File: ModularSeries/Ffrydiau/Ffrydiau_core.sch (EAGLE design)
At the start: 90 parts, among them IC3 556_DUALTIMERDIL14, Q1 2N3906, Q2 2N3904, Q3 2N3904, Q4 2N7000, Q5 2N7000, Q6 2N3904, Q7 2N3904, SW1 3XWIREPAD

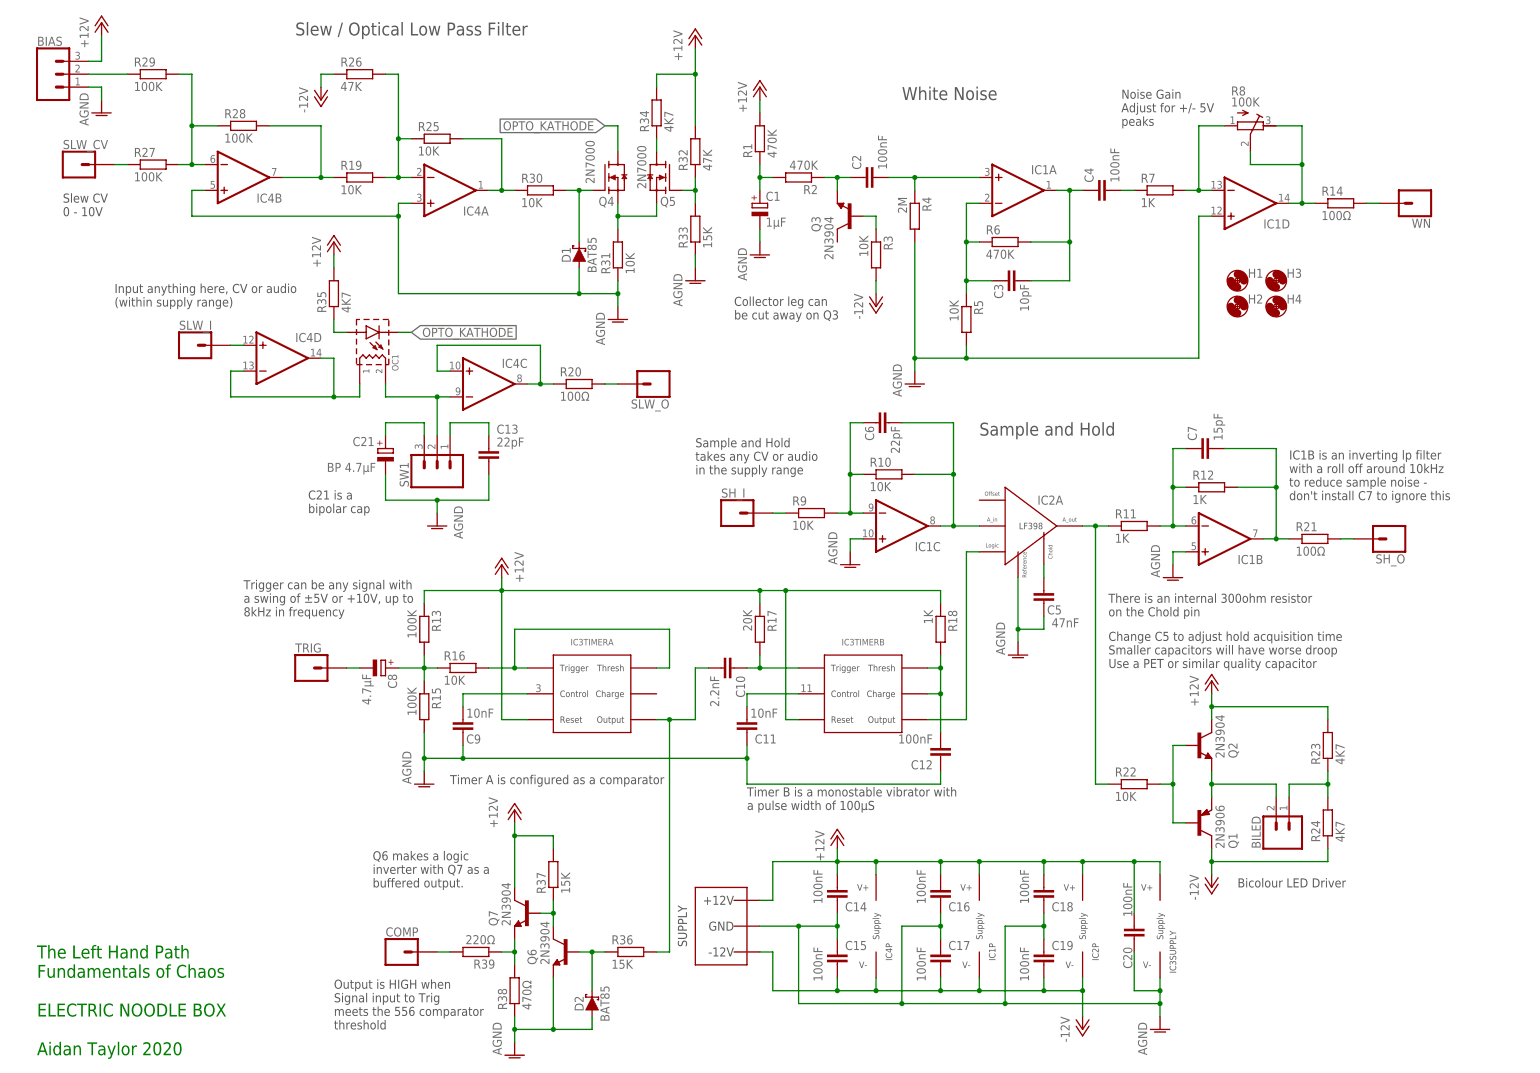
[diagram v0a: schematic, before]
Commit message: Portals BOM update, Ffrydiau project added
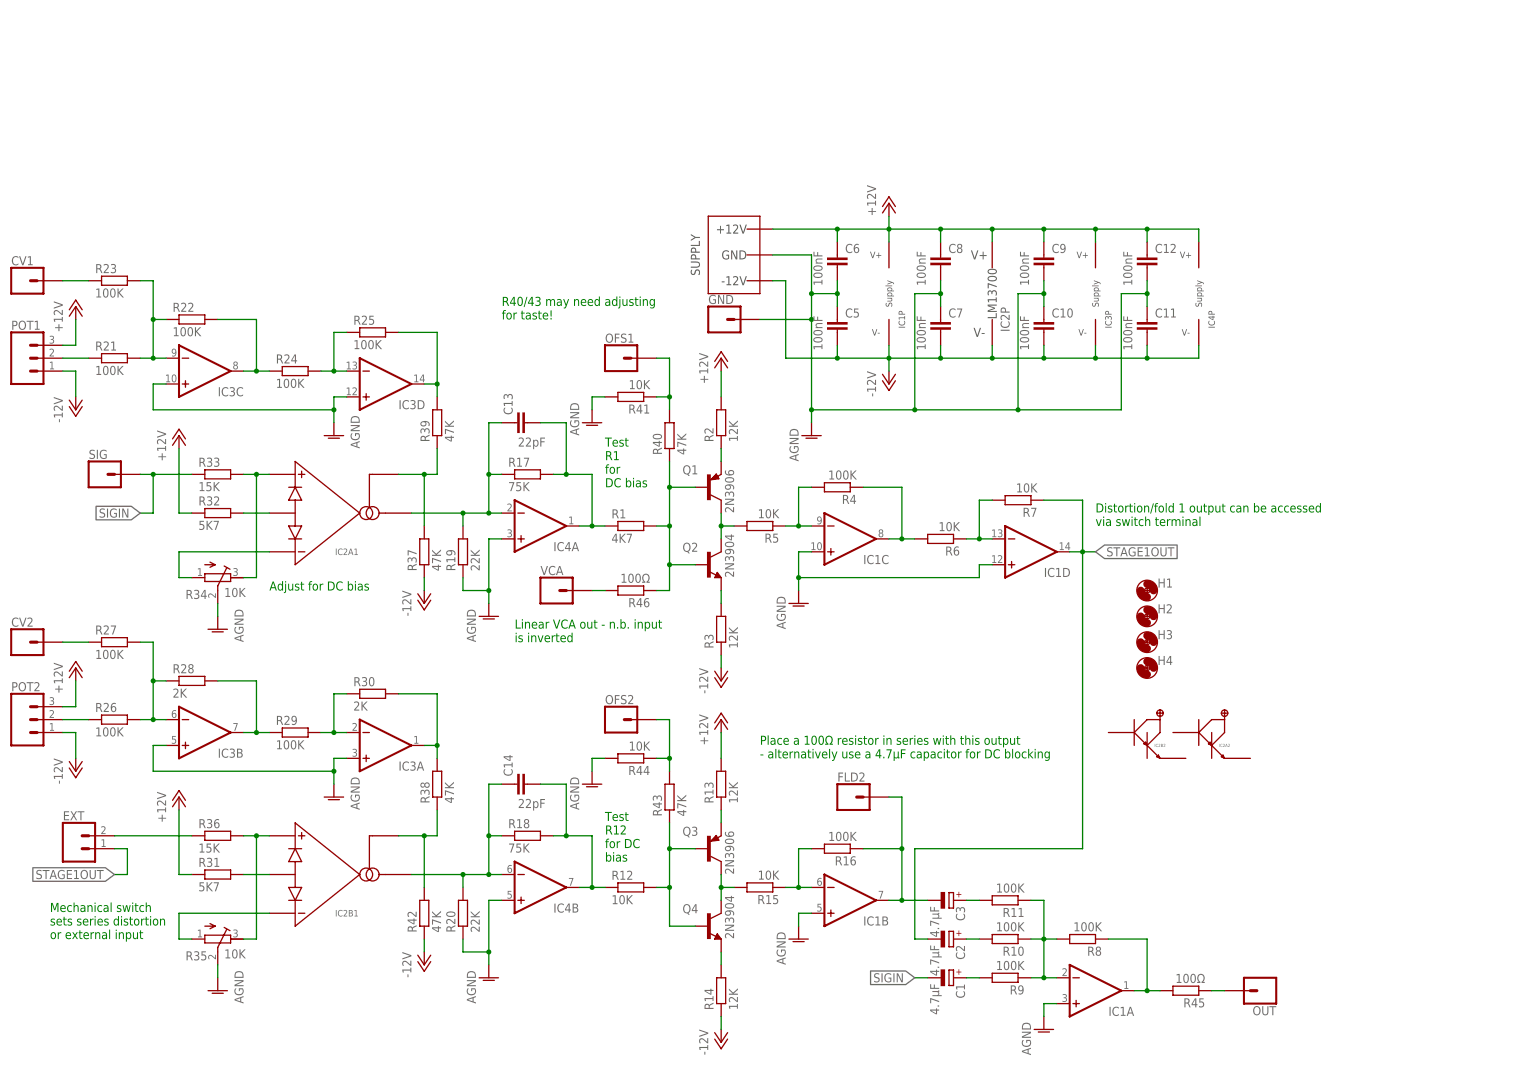
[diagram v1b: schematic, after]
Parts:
- removed BIAS, SW1: 3XWIREPAD, ElectricNoodleBox:3XWIREPAD
- removed BILED: 2XWIREPAD, ElectricNoodleBox:2XWIREPAD
- removed C15, C16, C17, C18, C19, C20, C4: 100nF, rcl:C-EU050-025X075
- removed C21: BP 4.7µF, rcl:CPOL-EUE2-5
- removed COMP, SH_I, SH_O, SLW_CV, SLW_I, SLW_O, TRIG, WN: 1XWIREPAD, ElectricNoodleBox:1XWIREPAD
- removed D1, D2: BAT85, ElectricNoodleBox:SCHOTTKY_DO35
- removed OC1: OPTOCOUPLERSILONEX, ElectricNoodleBox:OPTOCOUPLERSILONEX
- removed Q5: 2N7000, ElectricNoodleBox:2N7000
- removed Q6, Q7: 2N3904, transistor:2N3904
- added CV1, CV2, FLD2, GND, OFS1, OFS2, OUT, SIG, VCA: 1XWIREPAD, ElectricNoodleBox:1XWIREPAD
- added EXT: 2XWIREPAD, ElectricNoodleBox:2XWIREPAD
- added POT1, POT2: 3XWIREPAD, ElectricNoodleBox:3XWIREPAD
- added R40, R42, R43: 47K, rcl:R-EU_0207/10
- added R41, R44: 10K, rcl:R-EU_0207/10
- added R45, R46: 100Ω, rcl:R-EU_0207/10
- C1: value 1µF -> 4.7µF; device rcl:CPOL-EUE2-5 -> rcl:CPOL-EUE2,5-6E
- C10: value 2.2nF -> 100nF
- C11, C9: value 10nF -> 100nF
- C14: value 100nF -> 22pF
- C2: value 100nF -> 4.7µF; device rcl:C-EU050-025X075 -> rcl:CPOL-EUE2,5-6E
- C3: value 10pF -> 4.7µF; device rcl:C-EU050-025X075 -> rcl:CPOL-EUE2,5-6E
- C5: value 47nF -> 100nF
- C6: value 22pF -> 100nF
- C7: value 15pF -> 100nF
- C8: value 4.7µF -> 100nF; device rcl:CPOL-EUE2-5 -> rcl:C-EU050-025X075
- IC2: device ElectricNoodleBox:LF398 -> ElectricNoodleBox:LM13700DIL
- IC3: value 556_DUALTIMERDIL14 -> (none); device ElectricNoodleBox:556_DUALTIMERDIL14 -> ElectricNoodleBox:TL0X4DIL
- IC4: device ElectricNoodleBox:TL0X4DIL -> ElectricNoodleBox:TL0X2DIL
- Q2: device transistor:2N3904 -> transistor-npn:2N3904
- Q3: value 2N3904 -> 2N3906; device transistor:2N3904 -> transistor-pnp:2N3906
- Q4: value 2N7000 -> 2N3904; device ElectricNoodleBox:2N7000 -> transistor-npn:2N3904
- R1: value 470K -> 4K7; device rcl:R-EU_0207/7 -> rcl:R-EU_0207/10
- R10, R16, R22, R25, R9: value 10K -> 100K; device rcl:R-EU_0207/7 -> rcl:R-EU_0207/10
- R11: value 1K -> 100K; device rcl:R-EU_0207/7 -> rcl:R-EU_0207/10
- R12, R7: value 1K -> 10K; device rcl:R-EU_0207/7 -> rcl:R-EU_0207/10
- R13: value 100K -> 12K; device rcl:R-EU_0207/7 -> rcl:R-EU_0207/10
- R14: value 100Ω -> 12K; device rcl:R-EU_0207/7 -> rcl:R-EU_0207/10
- R15: value 100K -> 10K; device rcl:R-EU_0207/7 -> rcl:R-EU_0207/10
- R17: value 20K -> 75K; device rcl:R-EU_0207/7 -> rcl:R-EU_0207/10
- R18: value 1K -> 75K; device rcl:R-EU_0207/7 -> rcl:R-EU_0207/10
- R19: value 10K -> 22K; device rcl:R-EU_0207/7 -> rcl:R-EU_0207/10
- R2: value 470K -> 12K; device rcl:R-EU_0207/7 -> rcl:R-EU_0207/10
- R20: value 100Ω -> 22K; device rcl:R-EU_0207/7 -> rcl:R-EU_0207/10
- R21: value 100Ω -> 100K; device rcl:R-EU_0207/7 -> rcl:R-EU_0207/10
- R23, R24: value 4K7 -> 100K; device rcl:R-EU_0207/7 -> rcl:R-EU_0207/10
- R26: value 47K -> 100K; device rcl:R-EU_0207/7 -> rcl:R-EU_0207/10
- R27, R29, R33, R36, R5: device rcl:R-EU_0207/7 -> rcl:R-EU_0207/10
- R28: value 100K -> 2K; device rcl:R-EU_0207/7 -> rcl:R-EU_0207/10
- R3: value 10K -> 12K; device rcl:R-EU_0207/7 -> rcl:R-EU_0207/10
- R30: value 10K -> 2K; device rcl:R-EU_0207/7 -> rcl:R-EU_0207/10
- R31: value 10K -> 5K7; device rcl:R-EU_0207/7 -> rcl:R-EU_0207/10
- R32: value 47K -> 5K7; device rcl:R-EU_0207/7 -> rcl:R-EU_0207/10
- R34, R35: value 4K7 -> 10K; device rcl:R-EU_0207/7 -> rcl:R-TRIMM3296W
- R37: value 15K -> 47K; device rcl:R-EU_0207/7 -> rcl:R-EU_0207/10
- R38: value 470Ω -> 47K; device rcl:R-EU_0207/7 -> rcl:R-EU_0207/10
- R39: value 220Ω -> 47K; device rcl:R-EU_0207/7 -> rcl:R-EU_0207/10
- R4: value 2M -> 100K; device rcl:R-EU_0207/7 -> rcl:R-EU_0207/10
- R6: value 470K -> 10K; device rcl:R-EU_0207/7 -> rcl:R-EU_0207/10
- R8: device rcl:R-TRIMM3296W -> rcl:R-EU_0207/10
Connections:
- removed net N$48: BIAS.2, R29.1
- removed net N$49: Q6.C, Q7.B, R37.1
- removed net N$50: Q7.E, R38.2, R39.1
- removed net N$51: COMP.1, R39.2
- removed net N$52: D2.C, Q6.B, R36.1
- removed net OPTO_KATHODE: OC1.K, Q4.D
- new net SIGIN: C1.-, R33.1, SIG.1
- new net STAGE1OUT: C2.-, EXT.1, IC1D.OUT, R7.1
- net +12V: now also C12.1, C6.1, C8.1, C9.1, IC3P.V+, POT1.3, POT2.3, R13.2, R2.2, R31.1, R32.1; no longer BIAS.3, C14.2, C16.2, C18.2, C20.2, IC3SUPPLY.V+, IC3TIMERA.RESET, IC3TIMERB.RESET, Q2.C, Q7.C, R1.2, R13.1, R17.1, R18.1, R23.2, R32.2, R34.2, R35.2, R37.2
- net -12V: now also C10.2, C11.2, C5.2, C7.2, IC3P.V-, POT1.1, POT2.1, R14.1, R3.1, R37.1, R42.1; no longer C15.1, C17.1, C19.1, Q1.C, R24.1, R26.1, R3.2
- net AGND: now also C10.1, C12.2, C6.2, C7.1, C8.2, C9.2, GND.1, IC1A.+IN, IC3A.+IN, IC3B.+IN, IC3C.+IN, IC3D.+IN, R19.1, R20.1, R34.S, R35.S, R41.2, R44.2; no longer BIAS.1, C1.-, C12.1, C13.1, C14.1, C15.2, C16.1, C17.2, C18.1, C19.2, C20.1, C21.-, C9.1, D1.A, D2.A, IC2A.REFERENCE, IC3SUPPLY.V-, Q6.E, R15.2, R31.1, R33.1, R38.1, R4.2, R5.2
- net N$1: now also Q1.B, Q2.B, R1.2, R40.1, R46.1; no longer C1.+, R1.1, R2.2
- net N$10: now also C3.+, R11.2; no longer C6.1, IC1C.-IN, R10.1, R9.2
- net N$11: now also C2.+; no longer C6.2, IC1C.OUT, IC2A.ANALOG_IN
- net N$12: now also C1.+, R9.2; no longer C5.2, IC2A.CH
- net N$13: now also IC1A.-IN, R10.1, R8.2, R9.1; no longer IC2A.ANALOG_OUT, R22.1
- net N$14: now also IC1A.OUT, R45.2, R8.1; no longer C7.1, IC1B.-IN, R11.2, R12.1
- net N$15: now also Q3.B, Q4.B, R43.1; no longer C7.2, IC1B.OUT, R21.1
- net N$16: now also Q3.E, R13.1; no longer R9.1, SH_I.1
- net N$17: now also Q4.E, R14.2; no longer C10.2, IC3TIMERA.OUTPUT, R36.2
- net N$18: now also Q3.C, Q4.C, R15.2; no longer C8.+, R13.2, R15.1, R16.1
- net N$19: now also IC1B.-IN, R15.1; no longer IC3TIMERA.THRESHOLD, IC3TIMERA.TRIGGER
- net N$2: now also Q1.E; no longer C2.1, Q3.E
- net N$20: now also C3.-, FLD2.1, IC1B.OUT, R16.1; no longer R14.2, WN.1
- net N$21: now also C14.1, IC2B1.AMPOUT, IC4B.-IN, R18.1, R20.2; no longer C9.2, IC3TIMERA.CONT
- net N$22: now also C13.1, IC2A1.AMPOUT, IC4A.-IN, R17.1, R19.2; no longer C10.1, IC3TIMERB.TRIGGER, R17.2
- net N$23: now also C14.2, IC4B.OUT, R12.1, R18.2; no longer C11.2, IC3TIMERB.CONT
- net N$24: now also IC3C.-IN, R21.2, R22.1, R23.2; no longer C12.2, IC3TIMERB.DISCHARGE, IC3TIMERB.THRESHOLD, R18.2
- net N$25: now also IC3C.OUT, R22.2, R24.1; no longer IC2A.LOGIC, IC3TIMERB.OUTPUT
- net N$26: now also IC3D.-IN, R24.2, R25.1; no longer C8.-, TRIG.1
- net N$27: now also IC3D.OUT, R25.2, R39.2; no longer IC4D.+IN, SLW_I.1
- net N$28: now also CV2.1, R27.1; no longer IC4D.-IN, IC4D.OUT, OC1.R1
- net N$29: now also IC3A.OUT, R30.2, R38.2; no longer IC4B.OUT, R19.1, R28.2
- net N$3: now also Q2.E, R3.2; no longer Q3.B, R3.1
- net N$30: now also POT1.2, R21.1; no longer IC4C.-IN, OC1.R2, SW1.2
- net N$31: now also IC3A.-IN, R29.2, R30.1; no longer IC4C.+IN, IC4C.OUT, R20.1
- net N$32: now also CV1.1, R23.1; no longer R20.2, SLW_O.1
- net N$33: now also IC3B.OUT, R28.2, R29.1; no longer R21.2, SH_O.1
- net N$34: now also IC3B.-IN, R26.2, R27.2, R28.1; no longer Q1.B, Q2.B, R22.2
- net N$35: now also IC2B1.AMP+, R35.E, R36.2; no longer BILED.2, Q1.E, Q2.E
- net N$36: now also IC2B1.AMP-, R35.A; no longer BILED.1, R23.1, R24.2
- net N$37: now also IC2B1.DIODES, R31.2; no longer IC4A.-IN, R19.2, R25.1, R26.2
- net N$38: now also IC2A1.DIODES, R32.2; no longer IC4B.-IN, R27.2, R28.1, R29.2
- net N$39: now also IC2A1.AMPBIAS, R37.2, R39.1; no longer IC4A.OUT, R25.2, R30.1
- net N$4: now also Q1.C, Q2.C, R5.2; no longer C2.2, IC1A.+IN, R4.1
- net N$40: now also POT2.2, R26.1; no longer D1.C, Q4.G, R30.2
- net N$41: now also IC2A1.AMP+, R33.2, R34.E; no longer Q4.S, Q5.S, R31.2
- net N$42: now also IC2A1.AMP-, R34.A; no longer C21.+, SW1.3
- net N$43: now also IC2B1.AMPBIAS, R38.1, R42.2; no longer Q5.G, R32.1, R33.2
- net N$44: now also OFS1.1, R40.2, R41.1; no longer Q5.D, R34.1
- net N$45: now also OFS2.1, R43.2, R44.1; no longer OC1.A, R35.1
- net N$46: now also R46.2, VCA.1; no longer C13.2, SW1.1
- net N$47: now also EXT.2, R36.1; no longer R27.1, SLW_CV.1
- net N$5: now also IC1C.-IN, R4.2; no longer C3.1, IC1A.-IN, R6.1
- net N$6: now also IC1C.OUT, R4.1; no longer C3.2, C4.1, IC1A.OUT
- net N$7: now also IC1D.-IN, R6.1, R7.2; no longer C4.2, R7.1
- net N$8: now also OUT.1, R45.1; no longer IC1D.-IN, R7.2, R8.A
- net N$9: now also C13.2, IC4A.OUT, R1.1, R17.2; no longer IC1D.OUT, R14.1, R8.E, R8.S
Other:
- note added: "Adjust for DC bias"
- note added: "Distortion/fold 1 output can be accessed via switch terminal"
- note added: "Linear VCA out - n.b. input is inverted"
- note added: "Mechanical switch sets series distortion or external input"
- note added: "Place a 100Ω resistor in series with this output - alternatively use a 4.7µF capacitor for DC blocking"
- note added: "R40/43 may need adjusting for taste!"
- note added: "Test R1 for DC bias"
- note added: "Test R12 for DC bias"
- note removed: "Bicolour LED Driver"
- note removed: "C21 is a bipolar cap"
- note removed: "Change C5 to adjust hold acquisition time Smaller capacitors will have worse droop Use a PET or similar quality capacitor"
- note removed: "Collector leg can be cut away on Q3"
- note removed: "IC1B is an inverting lp filter with a roll off around 10kHz to reduce sample noise - don't install C7 to ignore this"
- note removed: "Input anything here, CV or audio (within supply range)"
- note removed: "Noise Gain Adjust for +/- 5V peaks"
- note removed: "Output is HIGH when Signal input to Trig meets the 556 comparator threshold"
- note removed: "Q6 makes a logic inverter with Q7 as a buffered output."
- note removed: "Sample and Hold"
- note removed: "Sample and Hold takes any CV or audio in the supply range"
- note removed: "Slew / Optical Low Pass Filter"
- note removed: "Slew CV 0 - 10V"
- note removed: "The Left Hand Path Fundamentals of Chaos ELECTRIC NOODLE BOX Aidan Taylor 2020"
- note removed: "There is an internal 300ohm resistor on the Chold pin"
- note removed: "Timer A is configured as a comparator"
- note removed: "Timer B is a monostable vibrator with a pulse width of 100µS"
- note removed: "Trigger can be any signal with a swing of ±5V or +10V, up to 8kHz in frequency"
- note removed: "White Noise"
- moved on the sheet: C1, C10, C11, C12, C13, C14, C5, C6, C7, C9, H1, H2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

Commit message: Ffrydiau renders for core PCB added
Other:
- note added: "Ffrydiau v1.0 Complex Wave Distortion Module Aidan Taylor 2020 ELECTRIC NOODLE BOX"
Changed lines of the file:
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@@
 sets series distortion
 or external input</text>
+<text x="127" y="0" size="2.54" layer="91">Ffrydiau v1.0
+Complex Wave Distortion Module
+Aidan Taylor 2020
+ELECTRIC NOODLE BOX</text>
 </plain>
 <instances>

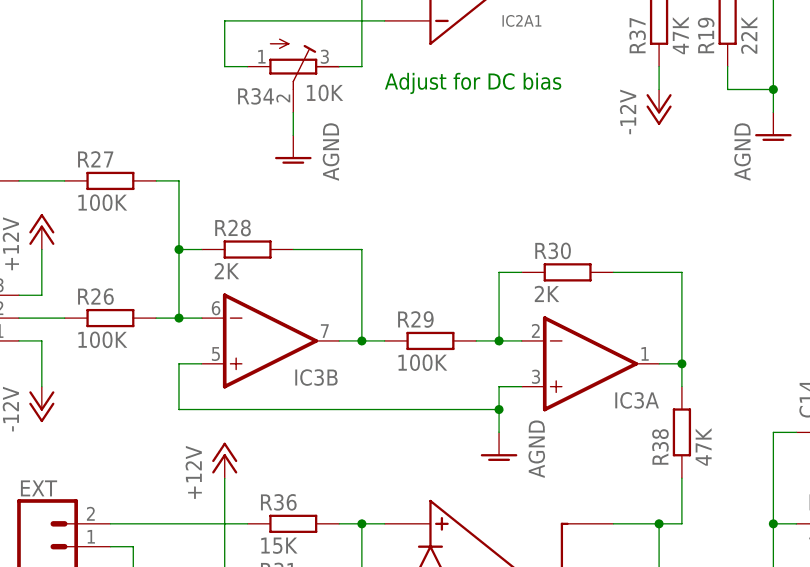
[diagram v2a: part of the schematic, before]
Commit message: Ffrydiau BOMs added
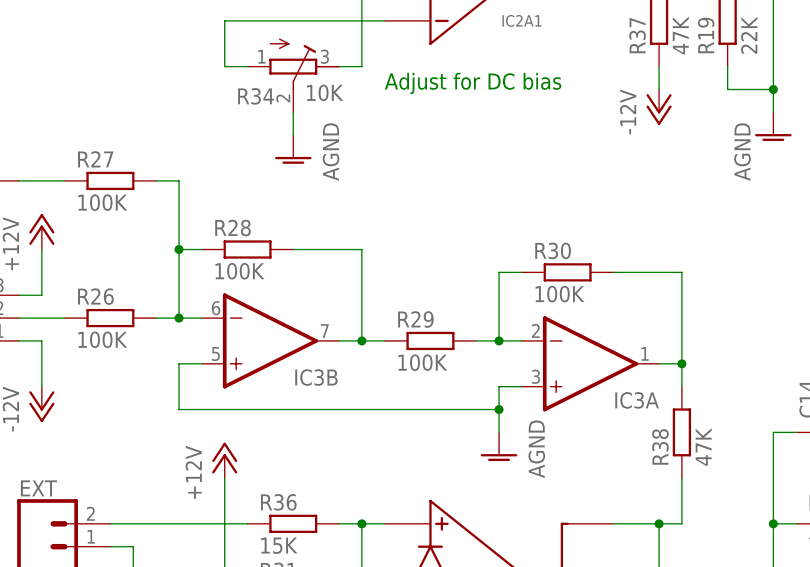
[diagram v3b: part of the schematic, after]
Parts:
- R28, R30: value 2K -> 100K
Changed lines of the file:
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@@
 <part name="R26" library="rcl" library_urn="urn:adsk.eagle:library:334" deviceset="R-EU_" device="0207/10" package3d_urn="urn:adsk.eagle:package:23491/2" value="100K"/>
 <part name="R27" library="rcl" library_urn="urn:adsk.eagle:library:334" deviceset="R-EU_" device="0207/10" package3d_urn="urn:adsk.eagle:package:23491/2" value="100K"/>
-<part name="R28" library="rcl" library_urn="urn:adsk.eagle:library:334" deviceset="R-EU_" device="0207/10" package3d_urn="urn:adsk.eagle:package:23491/2" value="2K"/>
+<part name="R28" library="rcl" library_urn="urn:adsk.eagle:library:334" deviceset="R-EU_" device="0207/10" package3d_urn="urn:adsk.eagle:package:23491/2" value="100K"/>
 <part name="R29" library="rcl" library_urn="urn:adsk.eagle:library:334" deviceset="R-EU_" device="0207/10" package3d_urn="urn:adsk.eagle:package:23491/2" value="100K"/>
-<part name="R30" library="rcl" library_urn="urn:adsk.eagle:library:334" deviceset="R-EU_" device="0207/10" package3d_urn="urn:adsk.eagle:package:23491/2" value="2K"/>
+<part name="R30" library="rcl" library_urn="urn:adsk.eagle:library:334" deviceset="R-EU_" device="0207/10" package3d_urn="urn:adsk.eagle:package:23491/2" value="100K"/>
 <part name="R31" library="rcl" library_urn="urn:adsk.eagle:library:334" deviceset="R-EU_" device="0207/10" package3d_urn="urn:adsk.eagle:package:23491/2" value="5K7"/>
 <part name="R32" library="rcl" library_urn="urn:adsk.eagle:library:334" deviceset="R-EU_" device="0207/10" package3d_urn="urn:adsk.eagle:package:23491/2" value="5K7"/>
